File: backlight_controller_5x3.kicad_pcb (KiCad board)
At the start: 2 copper layers, 121.3 x 67.3 mm, 50 parts, among them J1 DB9F_SMD, J10 M12-5_RCPT_F, J2 DB9M_SMD, J3 M12-5_RCPT_F, J4 M12-5_RCPT_F, J5 M12-5_RCPT_F, J6 M12-5_RCPT_F, J7 M12-5_RCPT_F, J8 M12-5_RCPT_F, J9 M12-5_RCPT_F, P1 MINI_FIT_JR_02X03_M_RA, U1 SN74ABT541BDWR, U2 SN74ABT541BDWR

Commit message: Finished version 1.1.
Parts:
- added U10: NUD3124, backlight_controller_5x3:TO-236-3, B.Cu at (178.4, 129.5)
- added U3: NUD3124, backlight_controller_5x3:TO-236-3, B.Cu at (121.3, 81.3)
- added U4: NUD3124, backlight_controller_5x3:TO-236-3, B.Cu at (121.3, 129.5)
- added U5: NUD3124, backlight_controller_5x3:TO-236-3, B.Cu at (140.3, 81.3)
- added U6: NUD3124, backlight_controller_5x3:TO-236-3, B.Cu at (140.3, 129.5)
- added U7: NUD3124, backlight_controller_5x3:TO-236-3, B.Cu at (159.4, 81.3)
- added U8: NUD3124, backlight_controller_5x3:TO-236-3, B.Cu at (159.4, 129.5)
- added U9: NUD3124, backlight_controller_5x3:TO-236-3, B.Cu at (178.4, 81.3)
- J10, J3, J4, J5, J6, J7, J8, J9: value M12-5_RCPT_F -> M12-5-RCPT_F_SMD; footprint backlight_controller_5x3:M12-5_RCPT_F -> footprints:M12-5_RCPT_F_SMD
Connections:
- J10 pad 2: (no net) -> /backlight_5x3/backlight_outputs/visible_3/NPN
- J10 pad 4: /backlight_5x3/C_15 -> (no net)
- J3 pad 2: (no net) -> /backlight_5x3/backlight_outputs/ir_0/NPN
- J3 pad 4: /backlight_5x3/C_8 -> (no net)
- J4 pad 2: (no net) -> /backlight_5x3/backlight_outputs/visible_0/NPN
- J4 pad 4: /backlight_5x3/C_9 -> (no net)
- J5 pad 2: (no net) -> /backlight_5x3/backlight_outputs/ir_1/NPN
- J5 pad 4: /backlight_5x3/C_10 -> (no net)
- J6 pad 2: (no net) -> /backlight_5x3/backlight_outputs/visible_1/NPN
- J6 pad 4: /backlight_5x3/C_11 -> (no net)
- J7 pad 2: (no net) -> /backlight_5x3/backlight_outputs/ir_2/NPN
- J7 pad 4: /backlight_5x3/C_12 -> (no net)
- J8 pad 2: (no net) -> /backlight_5x3/backlight_outputs/visible_2/NPN
- J8 pad 4: /backlight_5x3/C_13 -> (no net)
- J9 pad 2: (no net) -> /backlight_5x3/backlight_outputs/ir_3/NPN
- J9 pad 4: /backlight_5x3/C_14 -> (no net)
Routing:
- net GND: track 0.00 -> 621.1 mm
- net VAA: track 0.00 -> 294.8 mm, vias 0 -> 1
- net VEE: track 0.00 -> 130.9 mm, vias 0 -> 4
- net /~ENABLE: track 0.00 -> 112.6 mm
- net VDD: track 0.00 -> 98.1 mm, vias 0 -> 3
- net /backlight_5x3/C_1: track 0.00 -> 89.4 mm, vias 0 -> 1
- net /CHANNEL_0: track 0.00 -> 84.0 mm
- net /CHANNEL_15: track 0.00 -> 82.7 mm
- net /backlight_5x3/C_0: track 0.00 -> 80.7 mm
- net /CHANNEL_14: track 0.00 -> 79.3 mm
- net /CHANNEL_4: track 0.00 -> 78.2 mm
- net /CHANNEL_13: track 0.00 -> 76.0 mm
- net /CHANNEL_10: track 0.00 -> 75.7 mm
- net /CHANNEL_1: track 0.00 -> 74.2 mm
- net /CHANNEL_12: track 0.00 -> 73.1 mm, vias 0 -> 1
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- added copper zone on B.Cu, net GND
- added copper zone on F.Cu, net VAA

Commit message: high_power -> high_voltage. low_power -> low_voltage.
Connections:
- net /backlight_5x3/high_power_outputs/OUTPUT_0 renamed /backlight_5x3/high_voltage_outputs/OUTPUT_0
- net /backlight_5x3/high_power_outputs/OUTPUT_1 renamed /backlight_5x3/high_voltage_outputs/OUTPUT_1
- net /backlight_5x3/high_power_outputs/OUTPUT_2 renamed /backlight_5x3/high_voltage_outputs/OUTPUT_2
- net /backlight_5x3/high_power_outputs/OUTPUT_3 renamed /backlight_5x3/high_voltage_outputs/OUTPUT_3
- net /backlight_5x3/high_power_outputs/high_power_output_0/FAULT renamed /backlight_5x3/high_voltage_outputs/high_voltage_output_0/FAULT
- net /backlight_5x3/high_power_outputs/high_power_output_1/FAULT renamed /backlight_5x3/high_voltage_outputs/high_voltage_output_1/FAULT
- net /backlight_5x3/high_power_outputs/high_power_output_2/FAULT renamed /backlight_5x3/high_voltage_outputs/high_voltage_output_2/FAULT
- net /backlight_5x3/high_power_outputs/high_power_output_3/FAULT renamed /backlight_5x3/high_voltage_outputs/high_voltage_output_3/FAULT
- net /backlight_5x3/low_power_outputs/OUTPUT_0 renamed /backlight_5x3/low_voltage_outputs/OUTPUT_0
- net /backlight_5x3/low_power_outputs/OUTPUT_1 renamed /backlight_5x3/low_voltage_outputs/OUTPUT_1
- net /backlight_5x3/low_power_outputs/OUTPUT_2 renamed /backlight_5x3/low_voltage_outputs/OUTPUT_2
- net /backlight_5x3/low_power_outputs/OUTPUT_3 renamed /backlight_5x3/low_voltage_outputs/OUTPUT_3

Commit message: Progress towards v1.2.
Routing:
- net GND: track 621.1 -> 0.00 mm
- net VAA: track 294.8 -> 0.00 mm, vias 1 -> 0
- net VEE: track 130.9 -> 0.00 mm, vias 4 -> 0
- net /~ENABLE: track 112.6 -> 0.00 mm
- net VDD: track 98.1 -> 0.00 mm, vias 3 -> 0
- net /backlight_5x3/C_1: track 89.4 -> 0.00 mm, vias 1 -> 0
- net /CHANNEL_0: track 84.0 -> 0.00 mm
- net /CHANNEL_15: track 82.7 -> 0.00 mm
- net /backlight_5x3/C_0: track 80.7 -> 0.00 mm
- net /CHANNEL_14: track 79.3 -> 0.00 mm
- net /CHANNEL_4: track 78.2 -> 0.00 mm
- net /CHANNEL_13: track 76.0 -> 0.00 mm
- net /CHANNEL_10: track 75.7 -> 0.00 mm
- net /CHANNEL_1: track 74.2 -> 0.00 mm
- net /CHANNEL_12: track 73.1 -> 0.00 mm, vias 1 -> 0
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- removed copper zone on B.Cu, net GND
- removed copper zone on F.Cu, net VAA
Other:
- board text added: "High Voltage Channels"
- board text added: "Janelia Modular Device backlight_controller part_number: 1270 10/2018 ver 1.2 5x3"
- board text added: "Low Voltage Channels"
- board text removed: "High Power Channels"
- board text removed: "Janelia Modular Device backlight_controller part_number: 1270 10/2018 ver 1.1 5x3"
- board text removed: "Low Power Channels"

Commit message: Finished v1.2 schematic.
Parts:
- R5, R6, R7, R8: value 140 -> 75; footprint backlight_controller_5x3:SM1210 -> footprints:SM0805
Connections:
- MDB1 pad 14: /CHANNEL_8 -> /CHANNEL_5
- MDB1 pad 15: /CHANNEL_9 -> (no net)
- MDB1 pad 16: /CHANNEL_10 -> (no net)
- MDB1 pad 17: /CHANNEL_11 -> (no net)
- MDB1 pad 18: /CHANNEL_12 -> /CHANNEL_6
- MDB1 pad 19: /CHANNEL_13 -> /CHANNEL_7
- MDB1 pad 20: /CHANNEL_14 -> /CHANNEL_8
- MDB1 pad 21: /CHANNEL_15 -> /CHANNEL_9
- MDB1 pad 22: /CHANNEL_6 -> /CHANNEL_10
- MDB1 pad 23: /CHANNEL_7 -> /CHANNEL_11
- MDB1 pad 29: /CHANNEL_2 -> /CHANNEL_3
- MDB1 pad 30: /CHANNEL_3 -> /CHANNEL_4
- MDB1 pad 35: /CHANNEL_4 -> /CHANNEL_12
- MDB1 pad 36: /CHANNEL_5 -> /CHANNEL_13
- MDB1 pad 37: (no net) -> /CHANNEL_14
- MDB1 pad 38: (no net) -> /CHANNEL_15
- MDB1 pad 5: (no net) -> /CHANNEL_1
- MDB1 pad 6: /CHANNEL_1 -> /CHANNEL_2

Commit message: Finished version 1.2.
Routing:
- net GND: track 0.00 -> 618.1 mm
- net VAA: track 0.00 -> 293.7 mm, vias 0 -> 1
- net VEE: track 0.00 -> 141.2 mm, vias 0 -> 2
- net /CHANNEL_8: track 0.00 -> 95.1 mm
- net /backlight_5x3/C_0: track 0.00 -> 92.3 mm, vias 0 -> 2
- net /~ENABLE: track 0.00 -> 89.2 mm, vias 0 -> 3
- net /CHANNEL_11: track 0.00 -> 87.3 mm, vias 0 -> 1
- net /backlight_5x3/C_1: track 0.00 -> 84.9 mm, vias 0 -> 1
- net /CHANNEL_10: track 0.00 -> 84.3 mm, vias 0 -> 1
- net /CHANNEL_0: track 0.00 -> 84.0 mm
- net VDD: track 0.00 -> 82.7 mm
- net /CHANNEL_9: track 0.00 -> 82.0 mm
- net /CHANNEL_1: track 0.00 -> 76.8 mm
- net /CHANNEL_2: track 0.00 -> 72.6 mm
- net /backlight_5x3/C_9: track 0.00 -> 70.6 mm, vias 0 -> 1
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- added copper zone on B.Cu, net GND
- added copper zone on F.Cu, net VAA

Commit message: Prepare for version 1.3
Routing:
- net GND: track 618.1 -> 0.00 mm
- net VAA: track 293.7 -> 0.00 mm, vias 1 -> 0
- net VEE: track 141.2 -> 0.00 mm, vias 2 -> 0
- net /CHANNEL_8: track 95.1 -> 0.00 mm
- net /backlight_5x3/C_0: track 92.3 -> 0.00 mm, vias 2 -> 0
- net /~ENABLE: track 89.2 -> 0.00 mm, vias 3 -> 0
- net /CHANNEL_11: track 87.3 -> 0.00 mm, vias 1 -> 0
- net /backlight_5x3/C_1: track 84.9 -> 0.00 mm, vias 1 -> 0
- net /CHANNEL_10: track 84.3 -> 0.00 mm, vias 1 -> 0
- net /CHANNEL_0: track 84.0 -> 0.00 mm
- net VDD: track 82.7 -> 0.00 mm
- net /CHANNEL_9: track 82.0 -> 0.00 mm
- net /CHANNEL_1: track 76.8 -> 0.00 mm
- net /CHANNEL_2: track 72.6 -> 0.00 mm
- net /backlight_5x3/C_9: track 70.6 -> 0.00 mm, vias 1 -> 0
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- removed copper zone on B.Cu, net GND
- removed copper zone on F.Cu, net VAA
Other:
- board text added: "Janelia Modular Device backlight_controller part_number: 1270 05/2019 ver 1.3 5x3"
- board text removed: "Janelia Modular Device backlight_controller part_number: 1270 10/2018 ver 1.2 5x3"

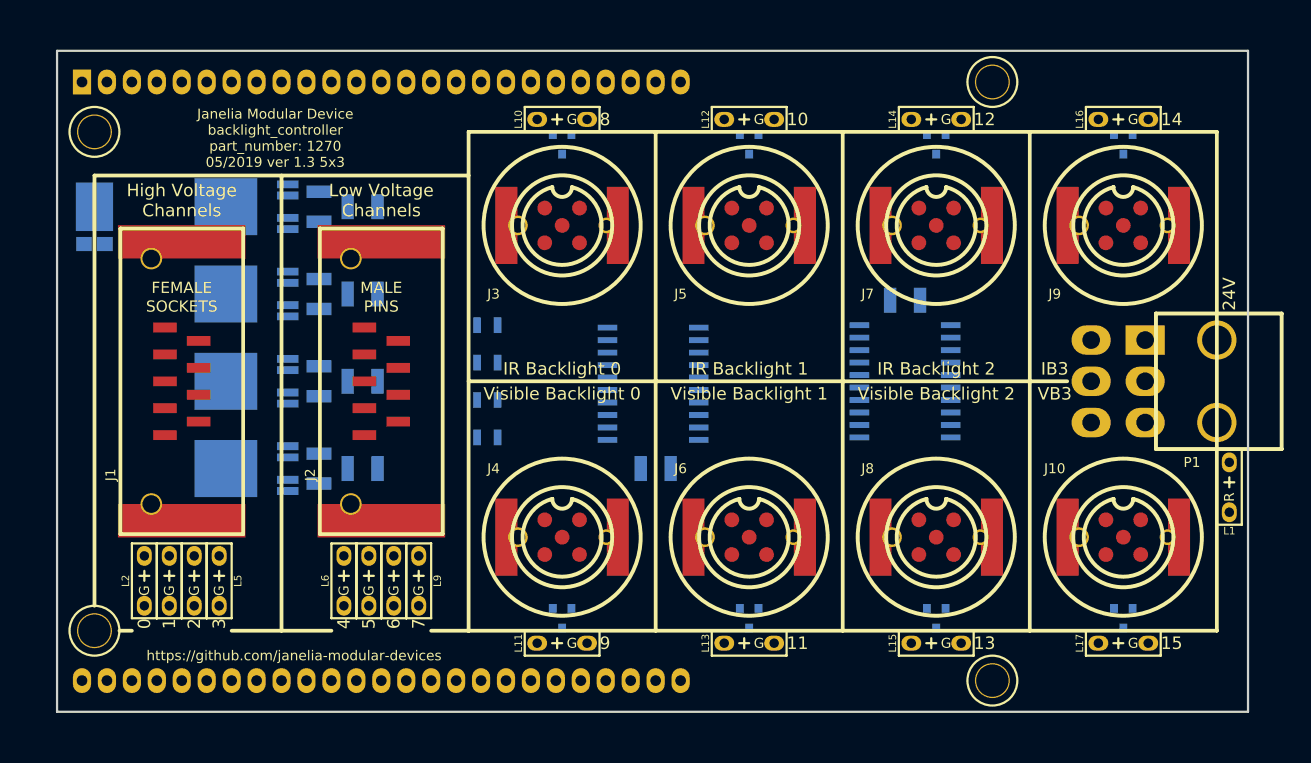
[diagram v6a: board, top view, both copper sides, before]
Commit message: Place footprints
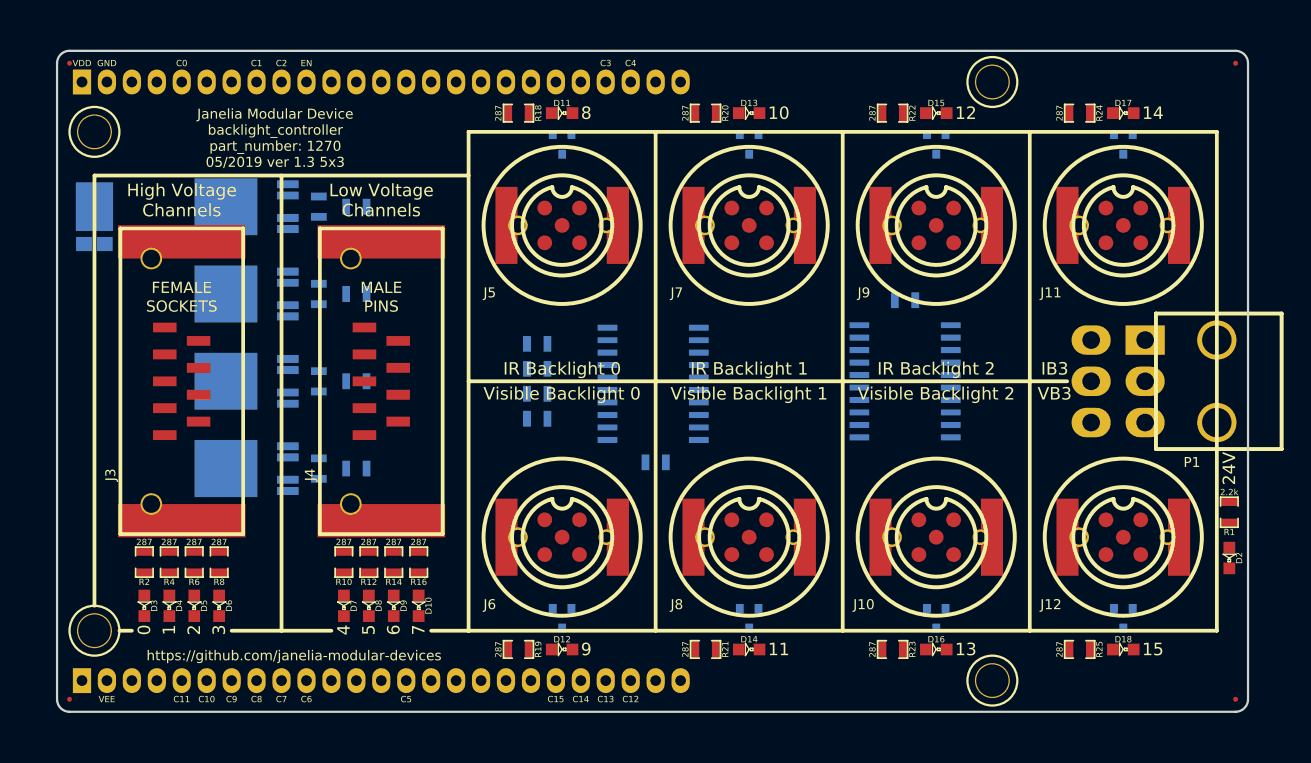
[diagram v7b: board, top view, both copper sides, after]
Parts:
- removed L1: LED_24V_RED, backlight_controller_5x3:LED_555-3XXX_R
- removed L10, L11, L12, L13, L14, L15, L16, L17, L2, L3, L4, L5, L6, L7, L8, L9: LED_5V_GRN, backlight_controller_5x3:LED_555-3XXX_G
- removed MDB1: MODULAR_DEVICE_BASE_5x3_MALE, backlight_controller_5x3:MODULAR_DEVICE_BASE_5X3_MALE
- added D10: LED_GRN, backlight_controller_5x3:LED0805, F.Cu at (106.7, 128.3)
- added D11: LED_GRN, backlight_controller_5x3:LED0805, F.Cu at (121.3, 78.1)
- added D12: LED_GRN, backlight_controller_5x3:LED0805, F.Cu at (121.3, 132.7)
- added D13: LED_GRN, backlight_controller_5x3:LED0805, F.Cu at (140.3, 78.1)
- added D14: LED_GRN, backlight_controller_5x3:LED0805, F.Cu at (140.3, 132.7)
- added D15: LED_GRN, backlight_controller_5x3:LED0805, F.Cu at (159.4, 78.1)
- added D16: LED_GRN, backlight_controller_5x3:LED0805, F.Cu at (159.4, 132.7)
- added D17: LED_GRN, backlight_controller_5x3:LED0805, F.Cu at (178.4, 78.1)
- added D18: LED_GRN, backlight_controller_5x3:LED0805, F.Cu at (178.4, 132.7)
- added D2: LED_GRN, backlight_controller_5x3:LED0805, F.Cu at (189.2, 123.4)
- added D3: LED_GRN, backlight_controller_5x3:LED0805, F.Cu at (78.7, 128.3)
- added D4: LED_GRN, backlight_controller_5x3:LED0805, F.Cu at (81.3, 128.3)
- added D5: LED_GRN, backlight_controller_5x3:LED0805, F.Cu at (83.8, 128.3)
- added D6: LED_GRN, backlight_controller_5x3:LED0805, F.Cu at (86.4, 128.3)
- added D7: LED_GRN, backlight_controller_5x3:LED0805, F.Cu at (99.1, 128.3)
- added D8: LED_GRN, backlight_controller_5x3:LED0805, F.Cu at (101.6, 128.3)
- added D9: LED_GRN, backlight_controller_5x3:LED0805, F.Cu at (104.1, 128.3)
- added FID1: FIDUCIAL, backlight_controller_5x3:FIDUCIAL, F.Cu at (71.1, 73.0)
- added FID2: FIDUCIAL, backlight_controller_5x3:FIDUCIAL, F.Cu at (189.9, 73.0)
- added FID3: FIDUCIAL, backlight_controller_5x3:FIDUCIAL, F.Cu at (189.9, 137.8)
- added FID4: FIDUCIAL, backlight_controller_5x3:FIDUCIAL, F.Cu at (71.1, 137.8)
- added J11: M12-5-RCPT, backlight_controller_5x3:M12-5_RCPT_F_SMD, F.Cu at (178.4, 89.5)
- added J12: M12-5-RCPT, backlight_controller_5x3:M12-5_RCPT_F_SMD, F.Cu at (178.4, 121.3)
- added MH1: MOUNTING_HOLE_4-40, backlight_controller_5x3:MOUNTING_HOLE_4-40, F.Cu at (73.7, 80.0)
- added MH2: MOUNTING_HOLE_4-40, backlight_controller_5x3:MOUNTING_HOLE_4-40, F.Cu at (165.1, 74.9)
- added MH3: MOUNTING_HOLE_4-40, backlight_controller_5x3:MOUNTING_HOLE_4-40, F.Cu at (165.1, 135.9)
- added MH4: MOUNTING_HOLE_4-40, backlight_controller_5x3:MOUNTING_HOLE_4-40, F.Cu at (73.7, 130.8)
- added R10: 287, backlight_controller_5x3:SM0805, F.Cu at (99.1, 123.8)
- added R11: 75, backlight_controller_5x3:SM0805, B.Cu at (118.7, 101.6)
- added R12: 287, backlight_controller_5x3:SM0805, F.Cu at (101.6, 123.8)
- added R13: 75, backlight_controller_5x3:SM0805, B.Cu at (118.7, 104.1)
- added R14: 287, backlight_controller_5x3:SM0805, F.Cu at (104.1, 123.8)
- added R15: 75, backlight_controller_5x3:SM0805, B.Cu at (118.7, 106.7)
- added R16: 287, backlight_controller_5x3:SM0805, F.Cu at (106.7, 123.8)
- added R17: 75, backlight_controller_5x3:SM0805, B.Cu at (118.7, 109.2)
- added R18: 287, backlight_controller_5x3:SM0805, F.Cu at (116.8, 78.1)
- added R19: 287, backlight_controller_5x3:SM0805, F.Cu at (116.8, 132.7)
- added R20: 287, backlight_controller_5x3:SM0805, F.Cu at (135.9, 78.1)
- added R21: 287, backlight_controller_5x3:SM0805, F.Cu at (135.9, 132.7)
- added R22: 287, backlight_controller_5x3:SM0805, F.Cu at (154.9, 78.1)
- added R23: 287, backlight_controller_5x3:SM0805, F.Cu at (154.9, 132.7)
- added R24: 287, backlight_controller_5x3:SM0805, F.Cu at (174.0, 78.1)
- added R25: 287, backlight_controller_5x3:SM0805, F.Cu at (174.0, 132.7)
- added R9: 5.9k, backlight_controller_5x3:SM0805, B.Cu at (100.3, 114.3)
- C1, C2, C3, C4, C5, C6, R3: footprint backlight_controller_5x3:SM1210 -> backlight_controller_5x3:SM0805
- D1: value diode_schottky_45V_10A -> DIODE_10A
- J1: value DB9F_SMD -> HEADER_01x25_MALE; footprint footprints:DB9F_SMD -> backlight_controller_5x3:HEADER_01x25; moved to B.Cu
- J10, J5, J6, J7, J8, J9: value M12-5-RCPT_F_SMD -> M12-5-RCPT; footprint footprints:M12-5_RCPT_F_SMD -> backlight_controller_5x3:M12-5_RCPT_F_SMD
- J2: value DB9M_SMD -> HEADER_01x25_MALE; footprint footprints:DB9M_SMD -> backlight_controller_5x3:HEADER_01x25; moved to B.Cu
- J3: value M12-5-RCPT_F_SMD -> DB9F; footprint footprints:M12-5_RCPT_F_SMD -> backlight_controller_5x3:DB9F_SMD
- J4: value M12-5-RCPT_F_SMD -> DB9M; footprint footprints:M12-5_RCPT_F_SMD -> backlight_controller_5x3:DB9M_SMD
- P1: value MINI_FIT_JR_02X03_M_RA -> MINI_FIT
- R1: value 5.9k -> 2.2k; footprint backlight_controller_5x3:SM1210 -> backlight_controller_5x3:SM0805; moved to F.Cu
- R2, R4: value 5.9k -> 287; footprint backlight_controller_5x3:SM1210 -> backlight_controller_5x3:SM0805; moved to F.Cu
- R5, R7: value 75 -> 5.9k; footprint footprints:SM0805 -> backlight_controller_5x3:SM0805
- R6, R8: value 75 -> 287; footprint footprints:SM0805 -> backlight_controller_5x3:SM0805; moved to F.Cu
- moved R1 93.6 mm to (189.2, 118.7)
- moved J3 41.9 mm to (82.5, 105.4), turned to 180 degrees
- moved J1 36.6 mm to (102.9, 74.9), turned to 0 degrees
- moved R6 36.1 mm to (83.8, 123.8)
- moved R2 35.2 mm to (78.7, 123.8)
- moved J2 30.5 mm to (102.9, 135.9), turned to 0 degrees
- moved R8 30.1 mm to (86.4, 123.8)
- moved J4 24.3 mm to (102.9, 105.4), turned to 180 degrees
- moved R4 21.9 mm to (81.3, 123.8)
- moved J10 19.1 mm to (159.4, 121.3), turned to 90 degrees
- moved J5 19.1 mm to (121.3, 89.5), turned to 90 degrees
- moved J6 19.1 mm to (121.3, 121.3), turned to 90 degrees
- moved J9 19.1 mm to (159.4, 89.5), turned to 90 degrees
- moved J7 19.0 mm to (140.3, 89.5), turned to 90 degrees
- moved J8 19.0 mm to (140.3, 121.3), turned to 90 degrees
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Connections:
- J1 pad 1: VAA -> VDD
- J1 pad 2: /backlight_5x3/high_voltage_outputs/OUTPUT_0 -> GND
- J1 pad 3: VAA -> (no net)
- J1 pad 4: /backlight_5x3/high_voltage_outputs/OUTPUT_1 -> (no net)
- J1 pad 5: VAA -> /CHANNEL_0
- J1 pad 6: /backlight_5x3/high_voltage_outputs/OUTPUT_2 -> (no net)
- J1 pad 7: VAA -> (no net)
- J1 pad 8: /backlight_5x3/high_voltage_outputs/OUTPUT_3 -> /CHANNEL_1
- J1 pad 9: VAA -> /CHANNEL_2
- J10 pad 2: /backlight_5x3/backlight_outputs/visible_3/NPN -> /backlight_5x3/backlight_outputs/visible_2/NPN
- J2 pad 1: GND -> (no net)
- J2 pad 2: /backlight_5x3/low_voltage_outputs/OUTPUT_0 -> VEE
- J2 pad 3: GND -> (no net)
- J2 pad 4: /backlight_5x3/low_voltage_outputs/OUTPUT_1 -> (no net)
- J2 pad 5: GND -> /CHANNEL_11
- J2 pad 6: /backlight_5x3/low_voltage_outputs/OUTPUT_2 -> /CHANNEL_10
- J2 pad 7: GND -> /CHANNEL_9
- J2 pad 8: /backlight_5x3/low_voltage_outputs/OUTPUT_3 -> /CHANNEL_8
- J2 pad 9: GND -> /CHANNEL_7
- J3 pad 2: /backlight_5x3/backlight_outputs/ir_0/NPN -> /backlight_5x3/high_voltage_outputs/OUTPUT_0
- J3 pad 3: GND -> VAA
- J3 pad 4: (no net) -> /backlight_5x3/high_voltage_outputs/OUTPUT_1
- J4 pad 1: VAA -> GND
- J4 pad 2: /backlight_5x3/backlight_outputs/visible_0/NPN -> /backlight_5x3/low_voltage_outputs/OUTPUT_0
- J4 pad 4: (no net) -> /backlight_5x3/low_voltage_outputs/OUTPUT_1
- J4 pad 5: VAA -> GND
- J5 pad 2: /backlight_5x3/backlight_outputs/ir_1/NPN -> /backlight_5x3/backlight_outputs/ir_0/NPN
- J6 pad 2: /backlight_5x3/backlight_outputs/visible_1/NPN -> /backlight_5x3/backlight_outputs/visible_0/NPN
- J7 pad 2: /backlight_5x3/backlight_outputs/ir_2/NPN -> /backlight_5x3/backlight_outputs/ir_1/NPN
- J8 pad 2: /backlight_5x3/backlight_outputs/visible_2/NPN -> /backlight_5x3/backlight_outputs/visible_1/NPN
- J9 pad 2: /backlight_5x3/backlight_outputs/ir_3/NPN -> /backlight_5x3/backlight_outputs/ir_2/NPN
- R1 pad 1: /backlight_5x3/high_voltage_outputs/high_voltage_output_0/FAULT -> VAA
- R1 pad 2: /backlight_5x3/C_0 -> Net-(D2-Pad1)
- R2 pad 1: /backlight_5x3/high_voltage_outputs/high_voltage_output_1/FAULT -> /backlight_5x3/C_0
- R2 pad 2: /backlight_5x3/C_1 -> Net-(D3-Pad1)
- R3 pad 1: /backlight_5x3/high_voltage_outputs/high_voltage_output_2/FAULT -> /backlight_5x3/C_0
- R3 pad 2: /backlight_5x3/C_2 -> /backlight_5x3/high_voltage_outputs/high_voltage_output_0/FAULT
- R4 pad 1: /backlight_5x3/high_voltage_outputs/high_voltage_output_3/FAULT -> /backlight_5x3/C_1
- R4 pad 2: /backlight_5x3/C_3 -> Net-(D4-Pad1)
- R5 pad 1: /backlight_5x3/low_voltage_outputs/OUTPUT_0 -> /backlight_5x3/C_1
- R5 pad 2: /backlight_5x3/C_4 -> /backlight_5x3/high_voltage_outputs/high_voltage_output_1/FAULT
- R6 pad 1: /backlight_5x3/low_voltage_outputs/OUTPUT_1 -> /backlight_5x3/C_2
- R6 pad 2: /backlight_5x3/C_5 -> Net-(D5-Pad1)
- R7 pad 1: /backlight_5x3/low_voltage_outputs/OUTPUT_2 -> /backlight_5x3/C_2
- R7 pad 2: /backlight_5x3/C_6 -> /backlight_5x3/high_voltage_outputs/high_voltage_output_2/FAULT
- R8 pad 1: /backlight_5x3/low_voltage_outputs/OUTPUT_3 -> /backlight_5x3/C_3
- R8 pad 2: /backlight_5x3/C_7 -> Net-(D6-Pad1)
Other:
- outline, holes or cut-outs redrawn
- board text added: "C0"
- board text added: "C1"
- board text added: "C10"
- board text added: "C11"
- board text added: "C12"
- board text added: "C13"
- board text added: "C14"
- board text added: "C15"
- board text added: "C2"
- board text added: "C3"
- board text added: "C4"
- board text added: "C5"
- board text added: "C6"
- board text added: "C7"
- board text added: "C8"
- board text added: "C9"
- board text added: "EN"
- board text added: "GND"
- board text added: "VDD"
- board text added: "VEE"

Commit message: Update documentation
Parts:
- moved R9 7.41 mm to (96.5, 120.7)
- moved HPS4 6.38 mm to (92.7, 120.7)
- moved R7 6.35 mm to (96.5, 110.5)
- moved R5 5.39 mm to (96.5, 100.3)
- moved HPS3 5.12 mm to (92.7, 110.5)
- moved R3 4.58 mm to (96.5, 90.2)
- moved C3 4.58 mm to (92.7, 85.1), turned to 0 degrees
- moved C4 4.02 mm to (92.7, 95.2), turned to 0 degrees
- moved C6 4.02 mm to (92.7, 115.6), turned to 0 degrees
- moved HPS2 3.86 mm to (92.7, 100.3)
- moved C5 3.81 mm to (92.7, 105.4), turned to 0 degrees
- moved HPS1 2.62 mm to (92.7, 90.2)
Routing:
- net GND: track 0.00 -> 757.9 mm, vias 0 -> 4
- net VAA: track 0.00 -> 338.4 mm, vias 0 -> 1
- net VEE: track 0.00 -> 125.6 mm, vias 0 -> 3
- net /CHANNEL_9: track 0.00 -> 95.2 mm
- net /CHANNEL_11: track 0.00 -> 92.2 mm
- net /~ENABLE: track 0.00 -> 90.0 mm, vias 0 -> 2
- net /CHANNEL_10: track 0.00 -> 86.7 mm
- net /CHANNEL_0: track 0.00 -> 84.0 mm
- net VDD: track 0.00 -> 82.0 mm
- net /backlight_5x3/C_13: track 0.00 -> 79.1 mm, vias 0 -> 1
- net /backlight_5x3/C_0: track 0.00 -> 78.5 mm, vias 0 -> 1
- net /CHANNEL_8: track 0.00 -> 76.8 mm, vias 0 -> 1
- net /CHANNEL_1: track 0.00 -> 76.8 mm
- net /backlight_5x3/C_1: track 0.00 -> 74.8 mm, vias 0 -> 3
- net /backlight_5x3/C_8: track 0.00 -> 71.5 mm, vias 0 -> 3
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- added copper zone on B.Cu, net GND
- added copper zone on F.Cu, net VAA
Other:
- rule pad_to_mask_clearance: 0 -> 0.1016
- rule solder_mask_min_width: 0.25 -> 0.1016
